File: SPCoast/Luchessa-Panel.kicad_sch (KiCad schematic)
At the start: 16 parts, among them SW8784 783, SW8796 795, SW8800 799, U8004 0x24, U8005 0x25, U8006 0x26

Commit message: refactor(kicad): model board lamps leave the columns; stale instance fields follow the libraries; PanelLamp-* retired
The owner's ruling (2026-10-23): the PanelColumn is the logical column, tied to a control point; the panel
I/O hardware is not. Every PanelLamp was a model board lamp except the maintainer-call lamp on the column's
pin 8. 34 lamps are now ModelLamp-<color> (no Column pin, Style board); 8 MC lamps are PanelMCall-Lamp.
Wires untouched: ~{LAMP} keeps its pin and the Column wire of a model lamp ends on nothing. Instance fields
the libraries dropped in c1d446b are gone from the sheets: Address on 7 processors, Interlocking and Machine
on 14 columns, Host on 2 transports. Railroad stays on the AAR encoding because its Topic template reads
${Railroad}; where Railroad lives is pending. Cached definitions refreshed for Processor, PanelColumn,
Transport-MQTT and Encoding-AAR. Scripted: SPCoast/edits/2026-10-23-model-lamps.py (edit, --check, --retire).

Verified: the script's gate on production/fields-after.net vs model-lamps-after.net: same 743 parts, lib ids
change only on the 42 lamps to the expected targets, fields change only as listed (Style indication->board
x34, the 37 drops), connectivity after == before minus the model lamps' pin 1, ERC 0 violations (the two
lib_symbol_mismatch warnings gone). lint_symbol_fields: 97 symbols, 0 errors (PanelLamp-BLUE, -GREEN, -RED, -YELLOW retired; there was no AMBER). Subdivision tests: 157 OK.

Co-Authored-By: Claude Fable 5.1 <noreply@anthropic.com>
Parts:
- COL8004, COL8005, COL8006: Interlocking Luchessa -> (none); Machine SPCoast South -> (none)
- LAMP8005, LAMP8007: symbol Railroad-Office:PanelLamp-RED -> Railroad-Office:ModelLamp-RED; Style indication -> board
- LAMP8006: symbol Railroad-Office:PanelLamp-YELLOW -> Railroad-Office:ModelLamp-YELLOW; Style indication -> board
- LAMP8008: symbol Railroad-Office:PanelLamp-YELLOW -> Railroad-Office:PanelMCall-Lamp
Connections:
- net at COL8004.1 (Column): no longer LAMP8005.1 (Column)
- net at COL8005.1 (Column): no longer LAMP8006.1 (Column)
- net at COL8005.2 (Column): no longer LAMP8007.1 (Column)
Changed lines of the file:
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@@
 	)
 	(symbol
-		(lib_id "Railroad-Office:PanelLamp-YELLOW")
+		(lib_id "Railroad-Office:PanelMCall-Lamp")
 		(at 132.08 132.08 0)
 		(unit 1)
@@
 			)
 		)
-		(property "Description" "One physical model board lamp. Value is a free descriptive label (e.g. OS, TRACK, MC) and is not used elsewhere. IndicationToken is a comma-separated list of indication names (track circuits such as 795T1,2NAA,799T1, or tokens such as MC1K) OR'd to drive this one lamp. All listed indications are still individually on the CodeLine wire"
+		(property "Description" "One physical Maintainer Call lamp.  IndicationToken is a comma-separated list of indication names (tokens such as MC1K)"
 			(at 132.08 139.7 0)
 			(hide yes)
@@
 	)
 	(symbol
-		(lib_id "Railroad-Office:PanelLamp-RED")
+		(lib_id "Railroad-Office:ModelLamp-RED")
 		(at 81.28 54.61 0)
 		(unit 1)
@@
 			)
 		)
-		(property "Description" "One physical model board lamp. Value is a free descriptive label (e.g. OS, TRACK, MC) and is not used elsewhere. IndicationToken is a comma-separated list of indication names (track circuits such as 795T1,2NAA,799T1, or tokens such as MC1K) OR'd to drive this one lamp. All listed indications are still individually on the CodeLine wire"
+		(property "Description" "One physical model board lamp. Value is a free descriptive label (e.g. OS, TRACK ...) and is not used elsewhere. IndicationToken is a comma-separated list of indication names (tokens from the CodeLine) OR'd to drive this one lamp."
 			(at 80.645 64.135 0)
 			(hide yes)
@@
 			)
 		)
-		(property "Style" "indication"
+		(property "Style" "board"
 			(at 81.28 57.15 0)
 			(hide yes)
@@
 				)
 			)
-		)
-		(pin "1"
 		)
 		(pin "2"
@@
 			)
 		)
-		(property "Interlocking" "Luchessa"
-			(at 132.08 157.48 0)
-			(show_name yes)
-			(do_not_autoplace yes)
-			(effects
-				(font
-					(size 1.27 1.27)
-				)
-			)
-		)
-		(property "Machine" "SPCoast South"
-			(at 132.715 153.67 0)
-			(show_name no)
-			(do_not_autoplace yes)
-			(effects
-				(font
-					(size 1.905 1.905)
-				)
-			)
-		)
 		(property "Role" "COLUMN"
 			(at 132.715 150.495 0)
@@
 	)
 	(symbol
-		(lib_id "Railroad-Office:PanelLamp-YELLOW")
+		(lib_id "Railroad-Office:ModelLamp-YELLOW")
 		(at 132.08 54.61 0)
 		(unit 1)
@@
 			)
 		)
-		(property "Description" "One physical model board lamp. Value is a free descriptive label (e.g. OS, TRACK, MC) and is not used elsewhere. IndicationToken is a comma-separated list of indication names (track circuits such as 795T1,2NAA,799T1, or tokens such as MC1K) OR'd to drive this one lamp. All listed indications are still individually on the CodeLine wire"
+		(property "Description" "One physical model board lamp. Value is a free descriptive label (e.g. OS, TRACK ...) and is not used elsewhere. IndicationToken is a comma-separated list of indication names (tokens from the CodeLine) OR'd to drive this one lamp."
 			(at 132.08 62.23 0)
 			(hide yes)
@@
 			)
 		)
-		(property "Style" "indication"
+		(property "Style" "board"
 			(at 132.08 52.07 0)
 			(hide yes)
@@
 				)
 			)
-		)
-		(pin "1"
 		)
 		(pin "2"
@@
 			)
 		)
-		(property "Interlocking" "Luchessa"
-			(at 182.88 157.48 0)
-			(show_name yes)
-			(do_not_autoplace yes)
-			(effects
-				(font
-					(size 1.27 1.27)
-				)
-			)
-		)
-		(property "Machine" "SPCoast South"
-			(at 183.515 153.67 0)
-			(show_name no)
-			(do_not_autoplace yes)
-			(effects
-				(font
-					(size 1.905 1.905)
-				)
-			)
-		)
 		(property "Role" "COLUMN"
 			(at 183.515 150.495 0)
@@
 	)
 	(symbol
-		(lib_id "Railroad-Office:PanelLamp-RED")
+		(lib_id "Railroad-Office:ModelLamp-RED")
 		(at 132.08 59.69 0)
 		(unit 1)
@@
 			)
 		)
-		(property "Description" "One physical model board lamp. Value is a free descriptive label (e.g. OS, TRACK, MC) and is not used elsewhere. IndicationToken is a comma-separated list of indication names (track circuits such as 795T1,2NAA,799T1, or tokens such as MC1K) OR'd to drive this one lamp. All listed indications are still individually on the CodeLine wire"
+		(property "Description" "One physical model board lamp. Value is a free descriptive label (e.g. OS, TRACK ...) and is not used elsewhere. IndicationToken is a comma-separated list of indication names (tokens from the CodeLine) OR'd to drive this one lamp."
 			(at 131.445 69.215 0)
 			(hide yes)
@@
 			)
 		)
-		(property "Style" "indication"
+		(property "Style" "board"
 			(at 132.08 62.23 0)
 			(hide yes)
@@
 				)
 			)
-		)
-		(pin "1"
 		)
 		(pin "2"
@@
 				)
 			)
-		)
-		(property "Interlocking" "Luchessa"
-			(at 81.28 157.48 0)
-			(show_name yes)
-			(do_not_autoplace yes)
-			(effects
-				(font
-					(size 1.27 1.27)
-				)
-			)
-		)
-		(property "Machine" "SPCoast South"
-			(at 81.915 153.67 0)
-			(show_name no)
-			(do_not_autoplace yes)
-			(effects
-				(font
-					(size 1.905 1.905)
-				)
-			)

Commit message: refactor(kicad): Name on every device, office unit and encoding; Kind on the JMRI drivers; Driver-JMRI-Light
The owner's rulings of 2026-10-24 on the review of ADR 0008 rev 4: Name = ${Value}
is the identity key everywhere, devices included; the OfficeUnit's Columns is
derived and struck; a JMRI driver carries no address and is keyed by its object
class and the device it serves, the class carried by Kind (TURNOUT, SENSOR,
SIGNALMAST, LIGHT); Driver-JMRI-Light (ADR 0005 §8: ON, INTENSITY) for a lamp
JMRI drives, and the two Gilroy Interchange maintainer-call lamps MC1 and MC2
become Lights (they were Sensors, which JMRI only displays).

Script: SPCoast/edits/2026-10-24-names-kind-light.py. Libraries: Name on 36
symbols (OfficeUnit, 5 encodings, 12 PANEL, 18 DEVICE), Columns off OfficeUnit,
Kind on 5 JMRI drivers, Driver-JMRI-Light added (the Sensor's pin positions,
INTENSITY as pin 3 below, no-connect on the two placed instances). Sheets: 359
Name instance fields, 16 Kind, 2 lib_id swaps, caches refreshed (no pin moved on
a refreshed symbol).

Verified: gate --check production/SPCoast.net production/names-after.net PASS:
same parts, same connectivity, Name == Value on all 273 named instances (47
heads with Value "~" resolve to an empty Name), Columns dropped once, Kind on 16
drivers, 2 Sensor -> Light with pin 1 reading ON; ERC 0 before and after.
Subdivision lint_symbol_fields: 99 symbols, 0 errors (Kind now allowed on
IODRIVER). production/SPCoast.net is the new export (production/ is untracked).

Co-Authored-By: Claude Fable 5.1 <noreply@anthropic.com>
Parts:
- AUX8002, CODE8002, LAMP8005, LAMP8006, LAMP8007, LAMP8008, SIG8785, SW8784, SW8796, SW8800: Name (none) -> ${Value}
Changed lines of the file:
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@@
 			)
 		)
+		(property "Name" "${Value}"
+			(at 81.28 111.76 0)
+			(hide yes)
+			(show_name no)
+			(do_not_autoplace no)
+			(effects
+				(font
+					(size 1.27 1.27)
+				)
+			)
+		)
 		(property "Appliance" "lever"
 			(at 81.28 120.65 0)
@@
 			)
 		)
+		(property "Name" "${Value}"
+			(at 81.28 91.44 0)
+			(hide yes)
+			(show_name no)
+			(do_not_autoplace no)
+			(effects
+				(font
+					(size 1.27 1.27)
+				)
+			)
+		)
 		(property "Appliance" "lever"
 			(at 81.915 104.14 0)
@@
 			)
 		)
+		(property "Name" "${Value}"
+			(at 132.08 132.08 0)
+			(hide yes)
+			(show_name no)
+			(do_not_autoplace no)
+			(effects
+				(font
+					(size 1.27 1.27)
+				)
+			)
+		)
 		(property "Appliance" "lamp"
 			(at 132.08 129.54 0)
@@
 			)
 		)
+		(property "Name" "${Value}"
+			(at 132.08 91.44 0)
+			(hide yes)
+			(show_name no)
+			(do_not_autoplace no)
+			(effects
+				(font
+					(size 1.27 1.27)
+				)
+			)
+		)
 		(property "Appliance" "lever"
 			(at 132.715 102.87 0)
@@
 			)
 		)
+		(property "Name" "${Value}"
+			(at 81.28 54.61 0)
+			(hide yes)
+			(show_name no)
+			(do_not_autoplace no)
+			(effects
+				(font
+					(size 1.27 1.27)
+				)
+			)
+		)
 		(property "Appliance" "lamp"
 			(at 81.28 57.15 0)
@@
 			)
 		)
+		(property "Name" "${Value}"
+			(at 81.28 91.44 0)
+			(hide yes)
+			(show_name no)
+			(do_not_autoplace no)
+			(effects
+				(font
+					(size 1.27 1.27)
+				)
+			)
+		)
 		(property "Appliance" "lever"
 			(at 81.915 104.14 0)
@@
 			)
 		)
+		(property "Name" "${Value}"
+			(at 132.08 54.61 0)
+			(hide yes)
+			(show_name no)
+			(do_not_autoplace no)
+			(effects
+				(font
+					(size 1.27 1.27)
+				)
+			)
+		)
 		(property "Appliance" "lamp"
 			(at 132.08 52.07 0)
@@
 			)
 		)
+		(property "Name" "${Value}"
+			(at 182.88 125.73 0)
+			(hide yes)
+			(show_name no)
+			(do_not_autoplace no)
+			(effects
+				(font
+					(size 1.27 1.27)
+				)
+			)
+		)
 		(property "Appliance" "lever"
 			(at 182.88 118.11 0)
@@
 			)
 		)
+		(property "Name" "${Value}"
+			(at 132.08 91.44 0)
+			(hide yes)
+			(show_name no)
+			(do_not_autoplace no)
+			(effects
+				(font
+					(size 1.27 1.27)
+				)
+			)
+		)
 		(property "Appliance" "lever"
 			(at 132.715 102.87 0)
@@
 			)
 		)
+		(property "Name" "${Value}"
+			(at 182.88 91.44 0)
+			(hide yes)
+			(show_name no)
+			(do_not_autoplace no)
+			(effects
+				(font
+					(size 1.27 1.27)
+				)
+			)
+		)
 		(property "Appliance" "lever"
 			(at 183.515 104.14 0)
@@
 			)
 		)
+		(property "Name" "${Value}"
+			(at 132.08 76.2 0)
+			(hide yes)
+			(show_name no)
+			(do_not_autoplace no)
+			(effects
+				(font
+					(size 1.27 1.27)
+				)
+			)
+		)
 		(property "Appliance" "lever"
 			(at 138.43 72.39 0)
@@
 			)
 		)
+		(property "Name" "${Value}"
+			(at 132.08 59.69 0)
+			(hide yes)
+			(show_name no)
+			(do_not_autoplace no)
+			(effects
+				(font
+					(size 1.27 1.27)
+				)
+			)
+		)
 		(property "Appliance" "lamp"
 			(at 132.08 62.23 0)
@@
 			)
 		)
+		(property "Name" "${Value}"
+			(at 81.28 111.76 0)
+			(hide yes)
+			(show_name no)
+			(do_not_autoplace no)
+			(effects
+				(font
+					(size 1.27 1.27)
+				)
+			)
+		)
 		(property "Appliance" "lever"
 			(at 81.28 120.65 0)
@@
 			(hide yes)
 			(show_name no)
+			(do_not_autoplace no)
+			(effects
+				(font
+					(size 1.27 1.27)
+				)
+			)
+		)
+		(property "Name" "${Value}"
+			(at 182.88 91.44 0)
+			(hide yes)
+			(show_name no)

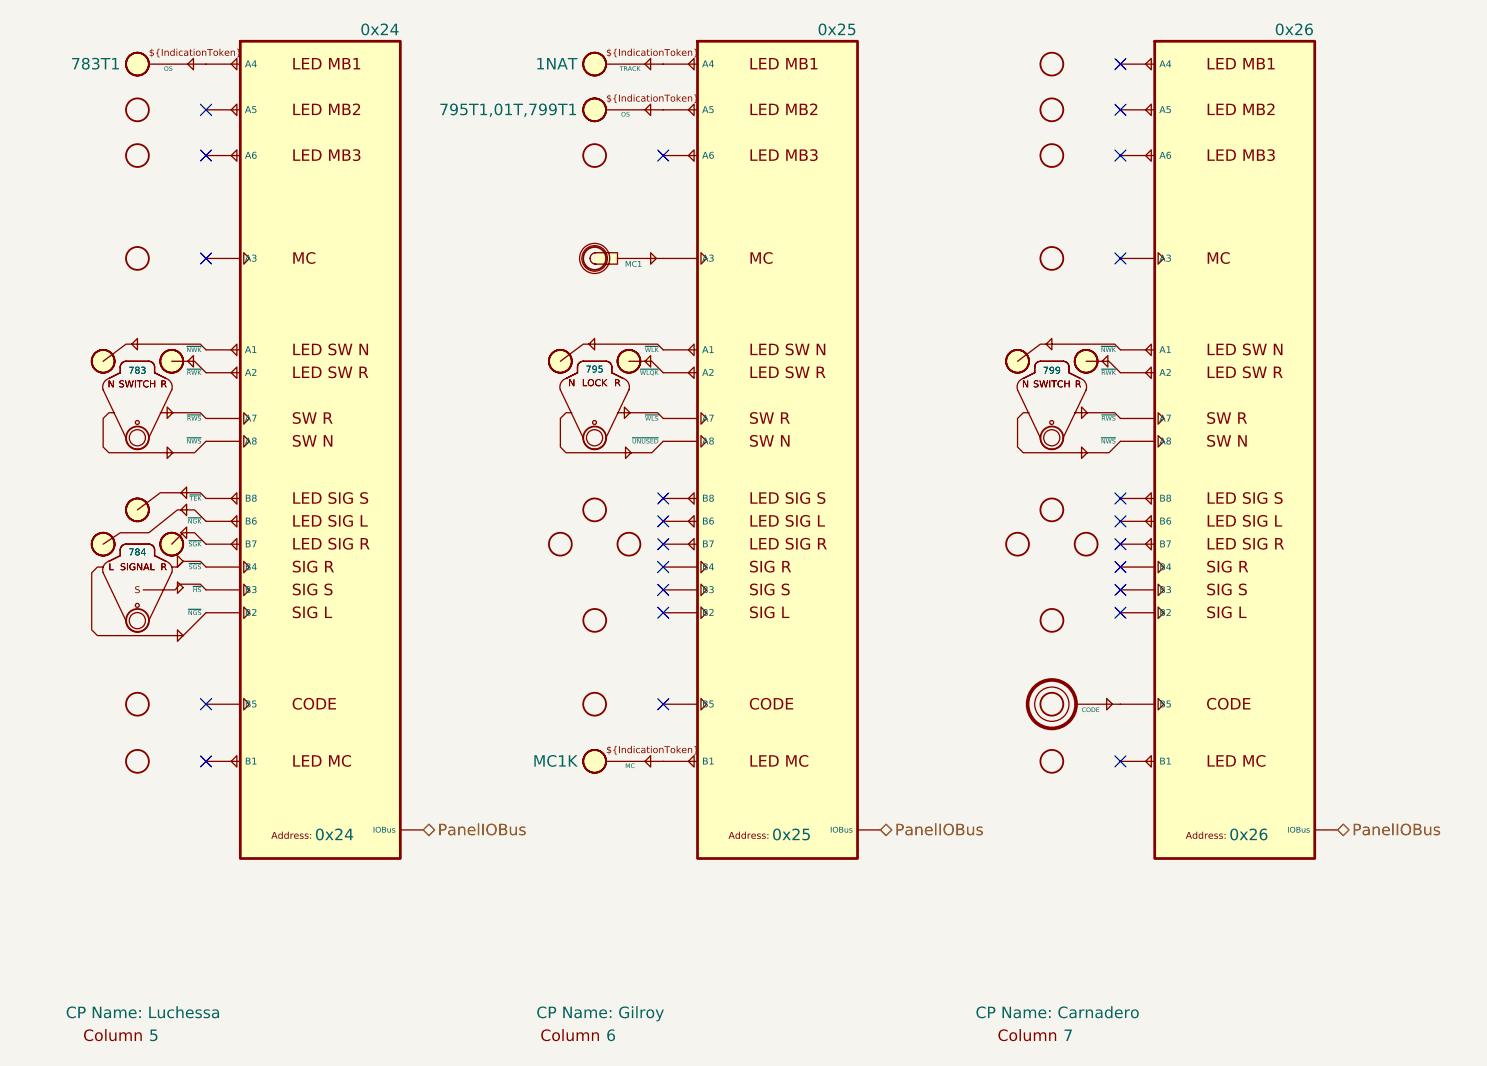
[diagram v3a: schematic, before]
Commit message: feat(spcoast): per-pin token fields on the panels, lamp Indication expressions, maintainer calls named 1MC
Applies the symbol rulings of 2026-10-28 to every sheet: the lib_symbols
caches of the changed symbols are the library's copies (this also clears
the stale PanelMCall and MaintainerCall caches), and every placed
instance gets the new hidden Control.*/Indication.* fields, loses
PanelLock Invert, and PanelMCall's whole-symbol Control and Indication
(Pin.MCK binary). Model lamps' IndicationToken becomes Indication: each
comma-separated circuit gets its K, qualifiers kept, joined with " | "
(795T1,01T,799T1 -> 795T1K | 01TK | 799T1K).

Maintainer calls in Christopher (1, 2), Corporal, Luchessa and Sargent
follow Gilroy Interchange (5dad54f): Value MC<n> -> <n>, Name ${Value}MC,
and the separate PanelMCall-Lamp is replaced by unit 2 of the same
PanelMCall at the old lamp's position, so its MCK pin sits where the
LAMP pin was. The old lamps' Column pin touched PanelColumn pin 8
directly (no wire); that pin is now unconnected, as on Gilroy
Interchange. Gilroy Interchange's local MaintainerCall_1 cache and its
two trackplan calls lose Indication.

Verified: fresh netlist before/after: components 752 -> 747 (the five
lamps), nets 1028 -> 1028; each old LAMP-pin net now holds the lever's
unit-2 MCK pin (pin 3) on the same expander pin (B1, pin 9); the levers'
nets are renamed only (~{S} -> ~{MCS}, unit suffix A); no other net
changed. Every field difference is an intended one. ERC 18 -> 1
violations (lib_symbol_mismatch 17 -> 0; pre-existing Sargent AUX1
pin_not_connected remains).

Co-Authored-By: Claude Opus 5.5 <noreply@anthropic.com>
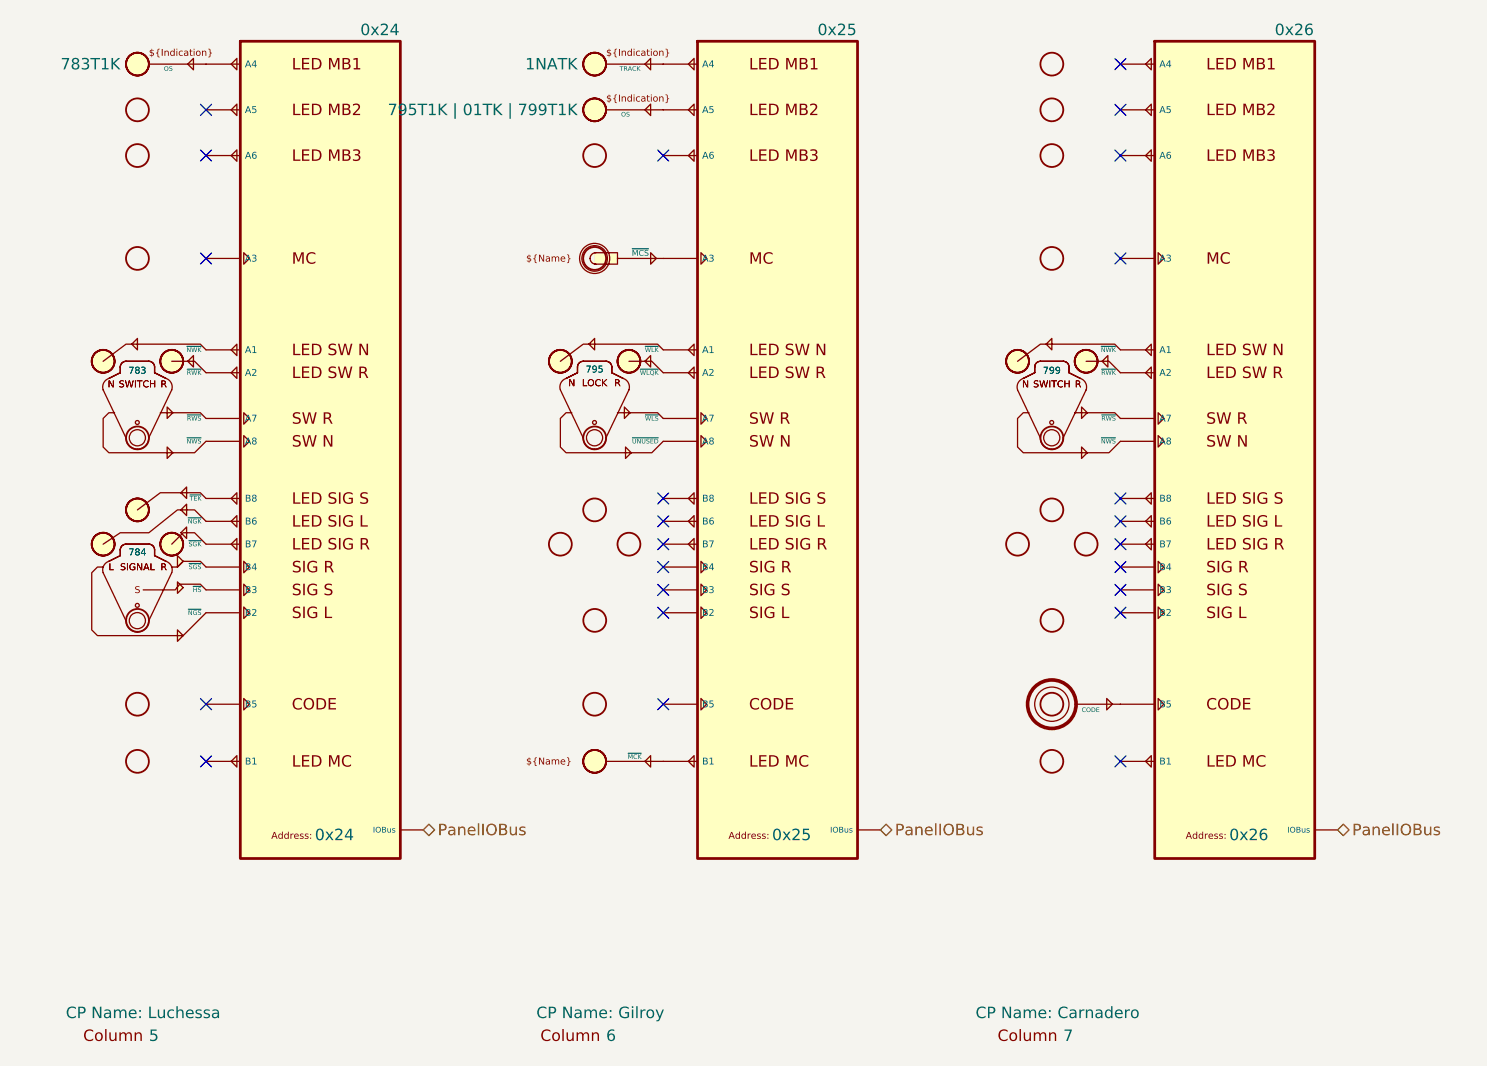
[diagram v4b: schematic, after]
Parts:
- removed LAMP8008: MC, symbol Railroad-Office:PanelMCall-Lamp
- added unit 2 of AUX8002
- AUX8002: value MC1 -> 1; Control.MCS (none) -> ${Value}MCS; Indication.MCK (none) -> ${Value}MCK; Name ${Value} -> ${Value}MC; Pin.MCK (none) -> binary; Pin.MCS (none) -> binary; Pin.S binary -> (none)
- LAMP8005: Indication (none) -> 783T1K; IndicationToken 783T1 -> (none)
- LAMP8006: Indication (none) -> 1NATK; IndicationToken 1NAT -> (none)
- LAMP8007: Indication (none) -> 795T1K | 01TK | 799T1K; IndicationToken 795T1,01T,799T1 -> (none)
- SIG8785: Control.HS (none) -> ${Value}HS; Control.NGS (none) -> ${Value}NGS; Control.SGS (none) -> ${Value}SGS; Indication.NGK (none) -> ${Value}NGK; Indication.SGK (none) -> ${Value}SGK; Indication.TEK (none) -> ${Value}TEK
- SW8784, SW8800: Control.NWS (none) -> ${Value}NWS; Control.RWS (none) -> ${Value}RWS; Indication.NWK (none) -> ${Value}NWK; Indication.RWK (none) -> ${Value}RWK
- SW8796: Control.WLS (none) -> ${Value}WLS; Indication.WLK (none) -> !${Value}WLK; Indication.WLQK (none) -> ${Value}WLQK; Invert WLK -> (none)
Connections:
- net at U8005.9 (B1): now also AUX8002.3 (~{MCK})
